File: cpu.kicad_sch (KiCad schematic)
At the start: 24 parts, among them J1 FTSH-105-01-L-DV-K, J24 HTSW-103-07-G-S, U4 CC2745P10, Y2 48MHZ 7PF 20ppm, Y4 32.768KHz 7pF 20ppm

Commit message: Change the cc2745 to a cc2755
Same pinout, cheaper, not automotive.

Signed-off-by: Corey Minyard <corey@minyard.net>
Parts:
- U4: value CC2745P10 -> CC2755P105E0WRHAR; symbol ICs:CC2745P10 -> Local ICs:CC2755P105E0WRHAR
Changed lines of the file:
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@@
 	)
 	(symbol
-		(lib_id "ICs:CC2745P10")
+		(lib_id "Local ICs:CC2755P105E0WRHAR")
 		(at 93.98 92.71 0)
 		(unit 1)
@@
 			)
 		)
-		(property "Value" "CC2745P10"
+		(property "Value" "CC2755P105E0WRHAR"
 			(at 125.73 83.82 0)
 			(effects

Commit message: Add some LEDs
Signed-off-by: Corey Minyard <corey@minyard.net>
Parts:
- added D4: YELLOW LED, LED_SMD:LED_0603_1608Metric_Pad1.05x0.95mm_HandSolder, symbol Device:LED
- added R39: 3KΩ, Resistor_SMD:R_0603_1608Metric_Pad0.98x0.95mm_HandSolder, symbol Device:R
- Y2: value 48MHZ 7PF 20ppm -> Crystal_GND24
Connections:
- net +3.3V: now also D4.2 (A)
- net at U4.3 (DIO0): now also R39.2
- new net: D4.1 (K), R39.1
- no-connect marks 3 -> 2
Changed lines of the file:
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@@
 	)
 	(junction
-		(at 179.07 157.48)
-		(diameter 0)
-		(color 0 0 0 0)
-	)
-	(junction
 		(at 167.64 43.18)
 		(diameter 0)
@@
 	)
 	(no_connect
-		(at 157.48 100.33)
-	)
-	(no_connect
 		(at 264.16 59.69)
 	)
@@
 	(wire
 		(pts
-			(xy 195.58 161.29) (xy 179.07 161.29)
+			(xy 157.48 100.33) (xy 190.5 100.33)
 		)
 		(stroke
@@
 	(wire
 		(pts
-			(xy 161.29 25.4) (xy 161.29 30.48)
+			(xy 195.58 161.29) (xy 179.07 161.29)
 		)
 		(stroke
@@
 	(wire
 		(pts
-			(xy 172.72 151.13) (xy 172.72 152.4)
+			(xy 161.29 25.4) (xy 161.29 30.48)
 		)
 		(stroke
@@
 	(wire
 		(pts
-			(xy 233.68 43.18) (xy 227.33 43.18)
+			(xy 172.72 151.13) (xy 172.72 152.4)
 		)
 		(stroke
@@
 	(wire
 		(pts
-			(xy 161.29 43.18) (xy 161.29 44.45)
+			(xy 233.68 43.18) (xy 227.33 43.18)
 		)
 		(stroke
@@
 	(wire
 		(pts
-			(xy 73.66 128.27) (xy 82.55 128.27)
+			(xy 161.29 43.18) (xy 161.29 44.45)
 		)
 		(stroke
@@
 	(wire
 		(pts
-			(xy 179.07 144.78) (xy 185.42 144.78)
+			(xy 73.66 128.27) (xy 82.55 128.27)
 		)
 		(stroke
@@
 	(wire
 		(pts
+			(xy 209.55 100.33) (xy 217.17 100.33)
+		)
+		(stroke
+			(width 0)
+			(type default)
+		)
+	)
+	(wire
+		(pts
 			(xy 90.17 95.25) (xy 90.17 92.71)
 		)
@@
 	(wire
 		(pts
-			(xy 185.42 144.78) (xy 185.42 146.05)
-		)
-		(stroke
-			(width 0)
-			(type default)
-		)
-	)
-	(wire
-		(pts
 			(xy 74.93 101.6) (xy 81.28 101.6)
 		)
@@
 	(wire
 		(pts
-			(xy 179.07 157.48) (xy 179.07 144.78)
-		)
-		(stroke
-			(width 0)
-			(type default)
-		)
-	)
-	(wire
-		(pts
 			(xy 220.98 38.1) (xy 220.98 43.18)
 		)
@@
 	(wire
 		(pts
+			(xy 217.17 100.33) (xy 217.17 97.79)
+		)
+		(stroke
+			(width 0)
+			(type default)
+		)
+	)
+	(wire
+		(pts
 			(xy 86.36 102.87) (xy 93.98 102.87)
 		)
@@
 	(wire
 		(pts
+			(xy 198.12 100.33) (xy 201.93 100.33)
+		)
+		(stroke
+			(width 0)
+			(type default)
+		)
+	)
+	(wire
+		(pts
 			(xy 54.61 146.05) (xy 93.98 146.05)
 		)
@@
 	)
 	(symbol
+		(lib_id "Device:LED")
+		(at 205.74 100.33 0)
+		(unit 1)
+		(exclude_from_sim no)
+		(in_bom yes)
+		(on_board yes)
+		(dnp no)
+		(property "Reference" "D4"
+			(at 209.042 101.346 0)
+			(effects
+				(font
+					(size 1.27 1.27)
+				)
+			)
+		)
+		(property "Value" "YELLOW LED"
+			(at 206.756 97.79 0)
+			(effects
+				(font
+					(size 1.27 1.27)
+				)
+			)
+		)
+		(property "Footprint" "LED_SMD:LED_0603_1608Metric_Pad1.05x0.95mm_HandSolder"
+			(at 205.74 100.33 0)
+			(effects
+				(font
+					(size 1.27 1.27)
+				)
+				(hide yes)
+			)
+		)
+		(property "Datasheet" "~"
+			(at 205.74 100.33 0)
+			(effects
+				(font
+					(size 1.27 1.27)
+				)
+				(hide yes)
+			)
+		)
+		(property "Description" "Light emitting diode"
+			(at 205.74 100.33 0)
+			(effects
+				(font
+					(size 1.27 1.27)
+				)
+				(hide yes)
+			)
+		)
+		(property "Sim.Pins" "1=K 2=A"
+			(at 205.74 100.33 0)
+			(effects
+				(font
+					(size 1.27 1.27)
+				)
+				(hide yes)
+			)
+		)
+		(pin "1"
+		)
+		(pin "2"
+		)
+		(instances
+			(project "FSKGroundStation"
+				(path "/23e49ab9-97e0-460a-806c-ff6f37958474/f1de8cbf-f219-47ea-9542-15169289ddba"
+					(reference "D4")
+					(unit 1)
+				)
+			)
+		)
+	)
+	(symbol
 		(lib_id "power:GND")
 		(at 74.93 111.76 0)
@@
 	)
 	(symbol
+		(lib_id "power:+3.3V")
+		(at 217.17 97.79 0)
+		(mirror y)
+		(unit 1)
+		(exclude_from_sim no)
+		(in_bom yes)
+		(on_board yes)
+		(dnp no)
+		(fields_autoplaced yes)
+		(property "Reference" "#PWR0151"
+			(at 217.17 101.6 0)
+			(effects
+				(font
+					(size 1.27 1.27)
+				)
+				(hide yes)
+			)
+		)
+		(property "Value" "+3.3V"
+			(at 217.17 92.71 0)
+			(effects
+				(font
+					(size 1.27 1.27)
+				)
+			)
+		)
+		(property "Footprint" ""
+			(at 217.17 97.79 0)
+			(effects
+				(font
+					(size 1.27 1.27)
+				)
+				(hide yes)
+			)
+		)
+		(property "Datasheet" ""
+			(at 217.17 97.79 0)
+			(effects
+				(font
+					(size 1.27 1.27)
+				)
+				(hide yes)
+			)
+		)
+		(property "Description" "Power symbol creates a global label with name \"+3.3V\""
+			(at 217.17 97.79 0)
+			(effects
+				(font
+					(size 1.27 1.27)
+				)
+				(hide yes)
+			)
+		)
+		(pin "1"
+		)
+		(instances
+			(project "FSKGroundStation"
+				(path "/23e49ab9-97e0-460a-806c-ff6f37958474/f1de8cbf-f219-47ea-9542-15169289ddba"
+					(reference "#PWR0151")
+					(unit 1)
+				)
+			)
+		)
+	)
+	(symbol
 		(lib_id "power:GND")
 		(at 195.58 85.09 0)
@@
 			)
 		)
-		(property "Value" "48MHZ 7PF 20ppm"
+		(property "Value" "Crystal_GND24"
 			(at 185.42 143.002 0)
 			(effects
@@
 					(unit 1)
 				)
+			)
+		)
+	)
+	(symbol
+		(lib_id "Device:R")
+		(at 194.31 100.33 270)
+		(unit 1)
+		(exclude_from_sim no)
+		(in_bom yes)
+		(on_board yes)
+		(dnp no)
+		(property "Reference" "R39"
+			(at 194.564 103.124 90)
+			(effects
+				(font
+					(size 1.27 1.27)
+				)
+			)
+		)
+		(property "Value" "3KΩ"
+			(at 194.31 97.79 90)
+			(effects
+				(font
+					(size 1.27 1.27)
+				)
+			)
+		)
+		(property "Footprint" "Resistor_SMD:R_0603_1608Metric_Pad0.98x0.95mm_HandSolder"
+			(at 194.31 98.552 90)
+			(effects
+				(font
+					(size 1.27 1.27)
+				)
+				(hide yes)
+			)
+		)
+		(property "Datasheet" "~"
+			(at 194.31 100.33 0)
+			(effects
+				(font
+					(size 1.27 1.27)
+				)
+				(hide yes)
+			)
+		)
+		(property "Description" "Resistor"
+			(at 194.31 100.33 0)
+			(effects
+				(font
+					(size 1.27 1.27)
+				)
+				(hide yes)
+			)
+		)
+		(pin "2"
+		)
+		(pin "1"
+		)
+		(instances
+			(project "FSKGroundStation"
+				(path "/23e49ab9-97e0-460a-806c-ff6f37958474/f1de8cbf-f219-47ea-9542-15169289ddba"
+					(reference "R39")
+					(unit 1)
+				)

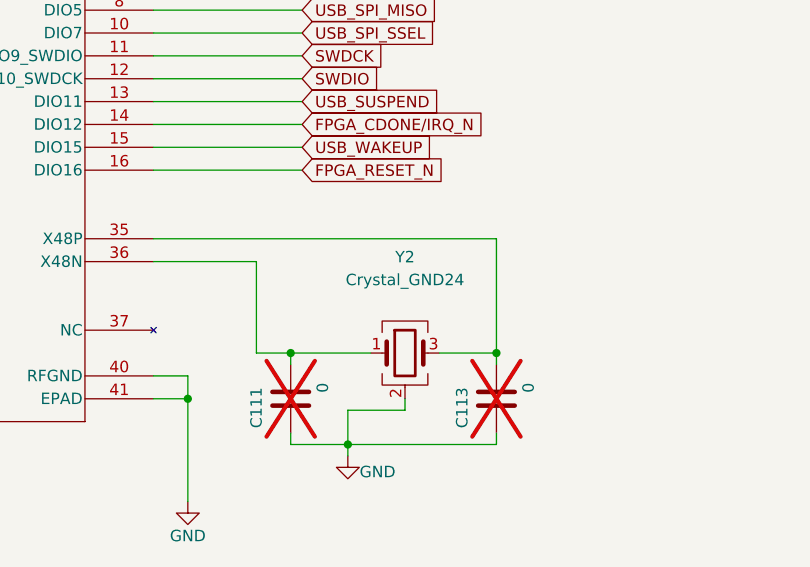
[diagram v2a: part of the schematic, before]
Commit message: Fix some components messed up by the previous change
Signed-off-by: Corey Minyard <corey@minyard.net>
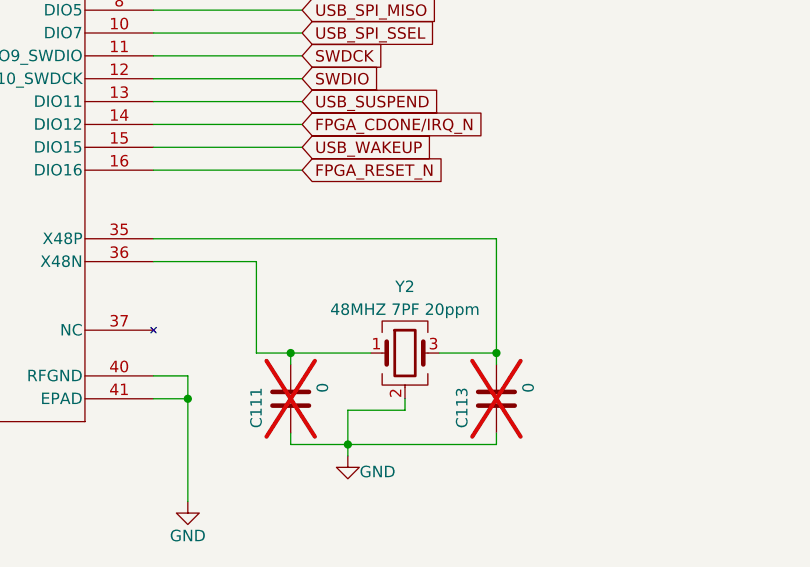
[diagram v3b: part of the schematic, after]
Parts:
- Y2: value Crystal_GND24 -> 48MHZ 7PF 20ppm
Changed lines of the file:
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@@
 		(dnp no)
 		(property "Reference" "Y2"
-			(at 185.42 140.462 0)
+			(at 185.42 143.764 0)
 			(effects
 				(font
@@
 			)
 		)
-		(property "Value" "Crystal_GND24"
-			(at 185.42 143.002 0)
+		(property "Value" "48MHZ 7PF 20ppm"
+			(at 185.42 146.304 0)
 			(effects
 				(font

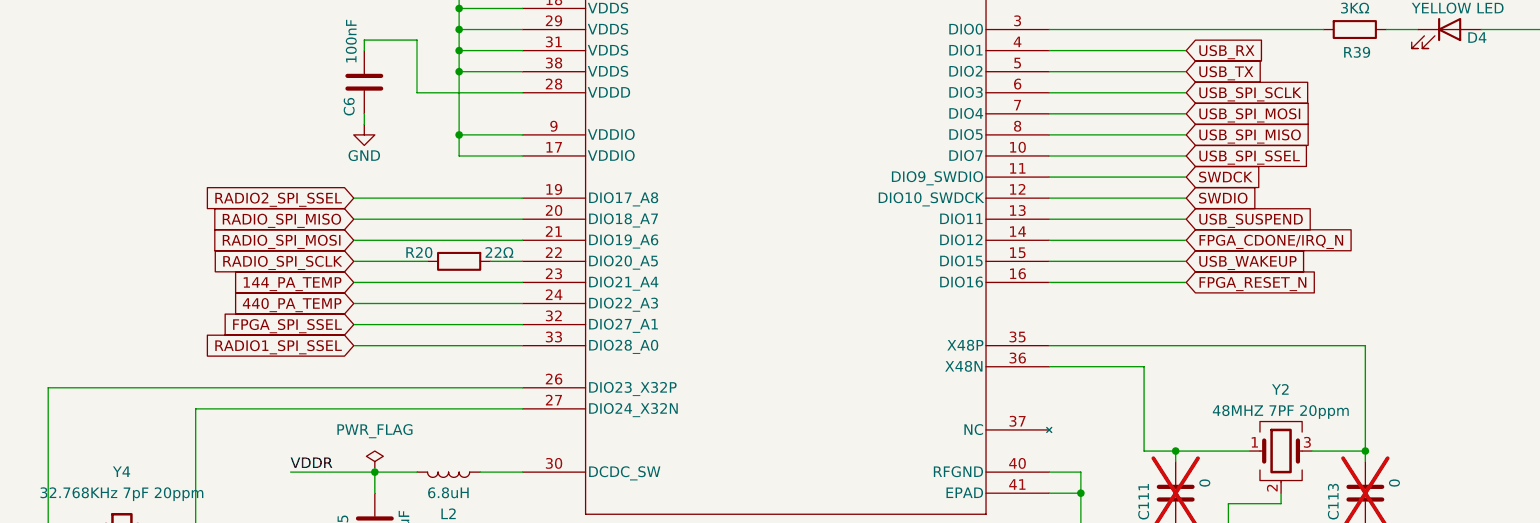
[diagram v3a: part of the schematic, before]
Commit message: Rewire the radio SPI pins
They couldn't go on the pins they were on.

Signed-off-by: Corey Minyard <corey@minyard.net>
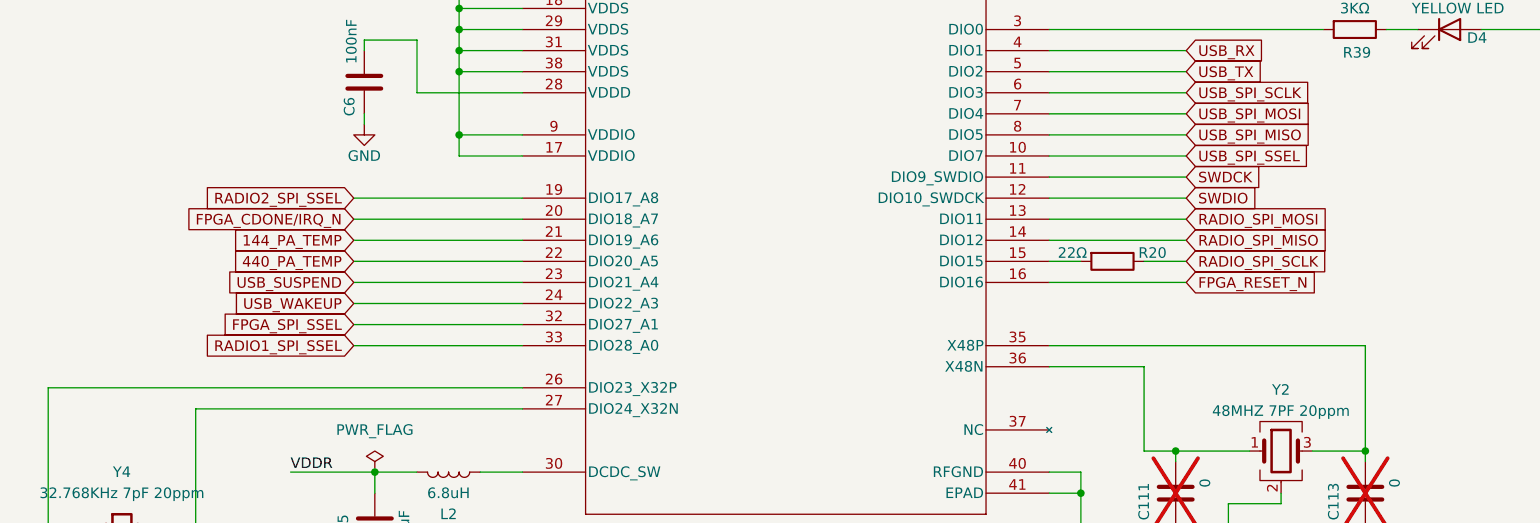
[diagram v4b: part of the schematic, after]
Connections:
- net 144_PA_TEMP: now also U4.21 (DIO19_A6); no longer U4.23 (DIO21_A4)
- net 440_PA_TEMP: now also U4.22 (DIO20_A5); no longer U4.24 (DIO22_A3)
- net FPGA_CDONE/IRQ_N: now also U4.20 (DIO18_A7); no longer U4.14 (DIO12)
- net RADIO_SPI_MISO: now also U4.14 (DIO12); no longer U4.20 (DIO18_A7)
- net RADIO_SPI_MOSI: now also U4.13 (DIO11); no longer U4.21 (DIO19_A6)
- net USB_SUSPEND: now also U4.23 (DIO21_A4); no longer U4.13 (DIO11)
- net USB_WAKEUP: now also U4.24 (DIO22_A3); no longer U4.15 (DIO15)
- net at R20.2: now also U4.15 (DIO15); no longer U4.22 (DIO20_A5)
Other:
- moved on the sheet: R20

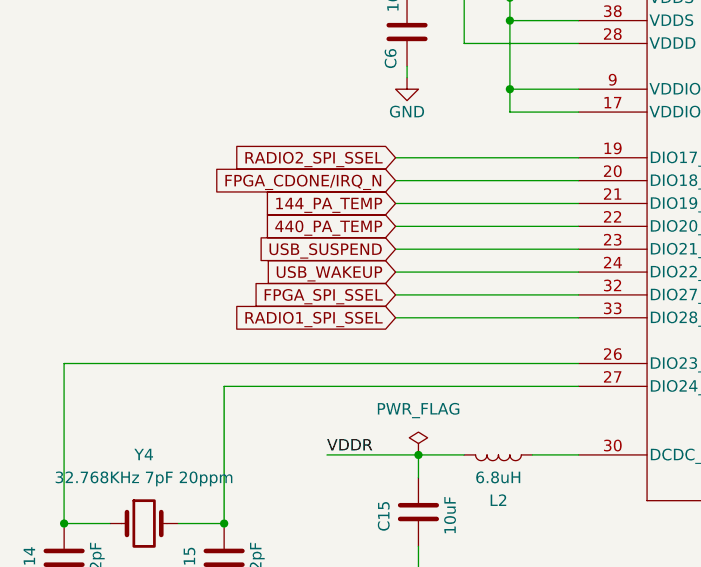
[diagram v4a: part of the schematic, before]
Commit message: More track cleanups for USB and the CPU
Make things a little neater.

Signed-off-by: Corey Minyard <corey@minyard.net>
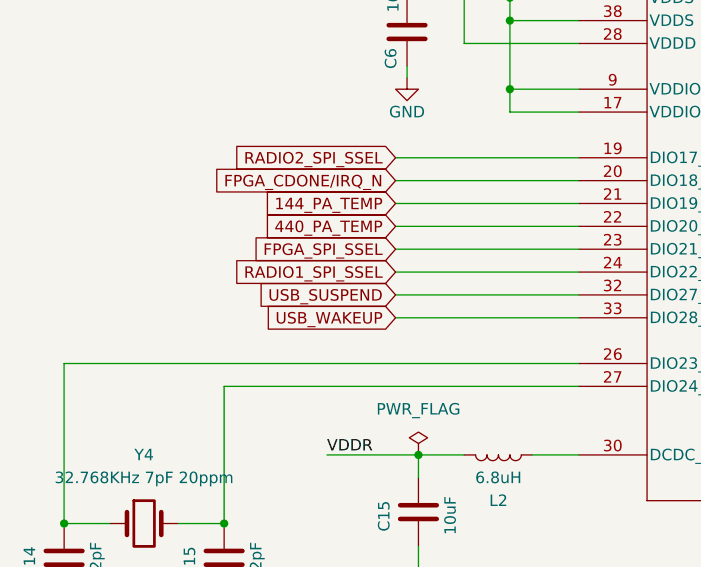
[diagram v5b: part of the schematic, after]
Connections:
- net FPGA_SPI_SSEL: now also U4.23 (DIO21_A4); no longer U4.32 (DIO27_A1)
- net RADIO1_SPI_SSEL: now also U4.24 (DIO22_A3); no longer U4.33 (DIO28_A0)
- net USB_SUSPEND: now also U4.32 (DIO27_A1); no longer U4.23 (DIO21_A4)
- net USB_WAKEUP: now also U4.33 (DIO28_A0); no longer U4.24 (DIO22_A3)

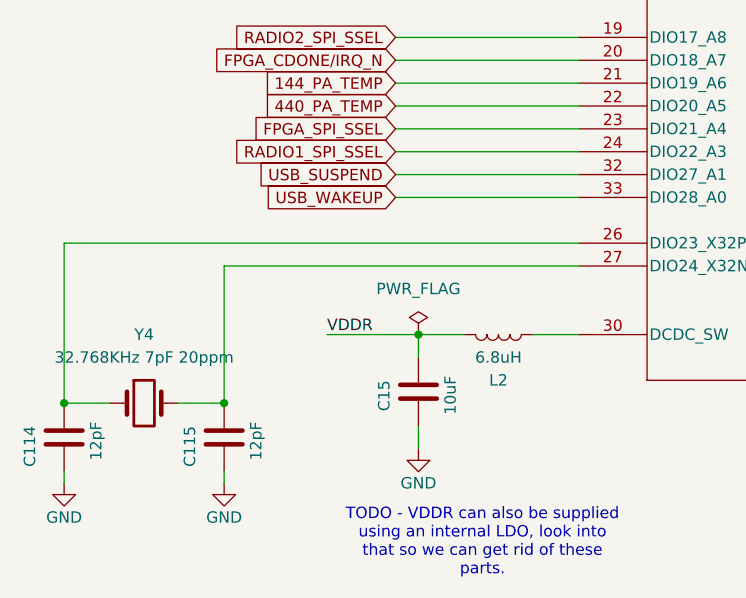
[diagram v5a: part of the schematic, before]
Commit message: Switch to a CPU with a USB interface for the USB connection
The part that was picked had proprietary tools and configuration and it
didn't support interrupts.  The CPU is cheaper and more capable.

Signed-off-by: Corey Minyard <corey@minyard.net>
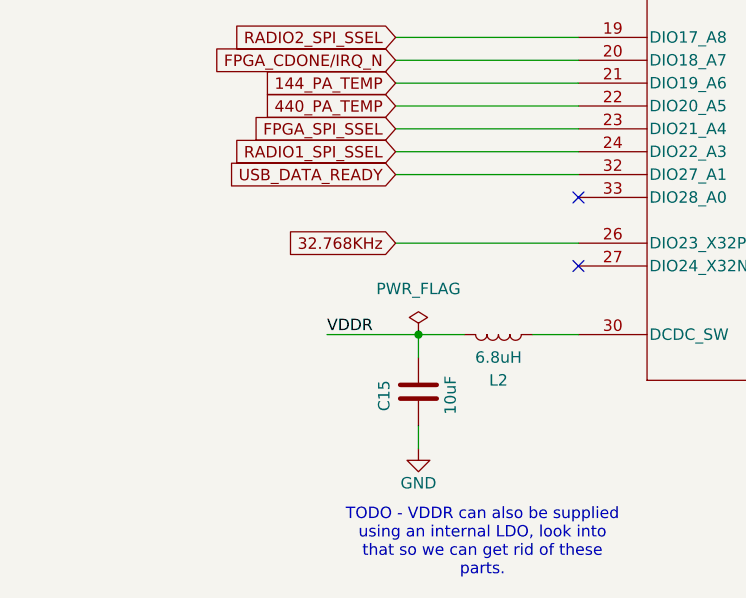
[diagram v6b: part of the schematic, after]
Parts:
- removed C114, C115: 12pF, Capacitor_SMD:C_0402_1005Metric_Pad0.74x0.62mm_HandSolder, symbol Device:C
- removed Y4: 32.768KHz 7pF 20ppm, Crystal:Crystal_SMD_2012-2Pin_2.0x1.2mm, symbol Device:Crystal
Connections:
- net 32.768KHz: now reaches U4.26 (DIO23_X32P)
- net USB_SUSPEND renamed USB_DATA_READY
- net USB_WAKEUP: no longer names the net of U4.33 (DIO28_A0)
- no-connect marks 2 -> 4

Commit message: Add a clock from the USB chip to the FPGA
The FPGA might need a clock for certain things, so provide it.

Signed-off-by: Corey Minyard <corey@minyard.net>
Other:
- note added: "The USB interface provides a 32.768KHz clock, we use that here."
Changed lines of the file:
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@@
+		)
+	)
+	(text "The USB interface provides a\n32.768KHz clock, we use that\nhere."
+		(exclude_from_sim no)
+		(at 44.45 144.272 0)
+		(effects
+			(font
+				(size 1.27 1.27)
+			)
 		)
 	)

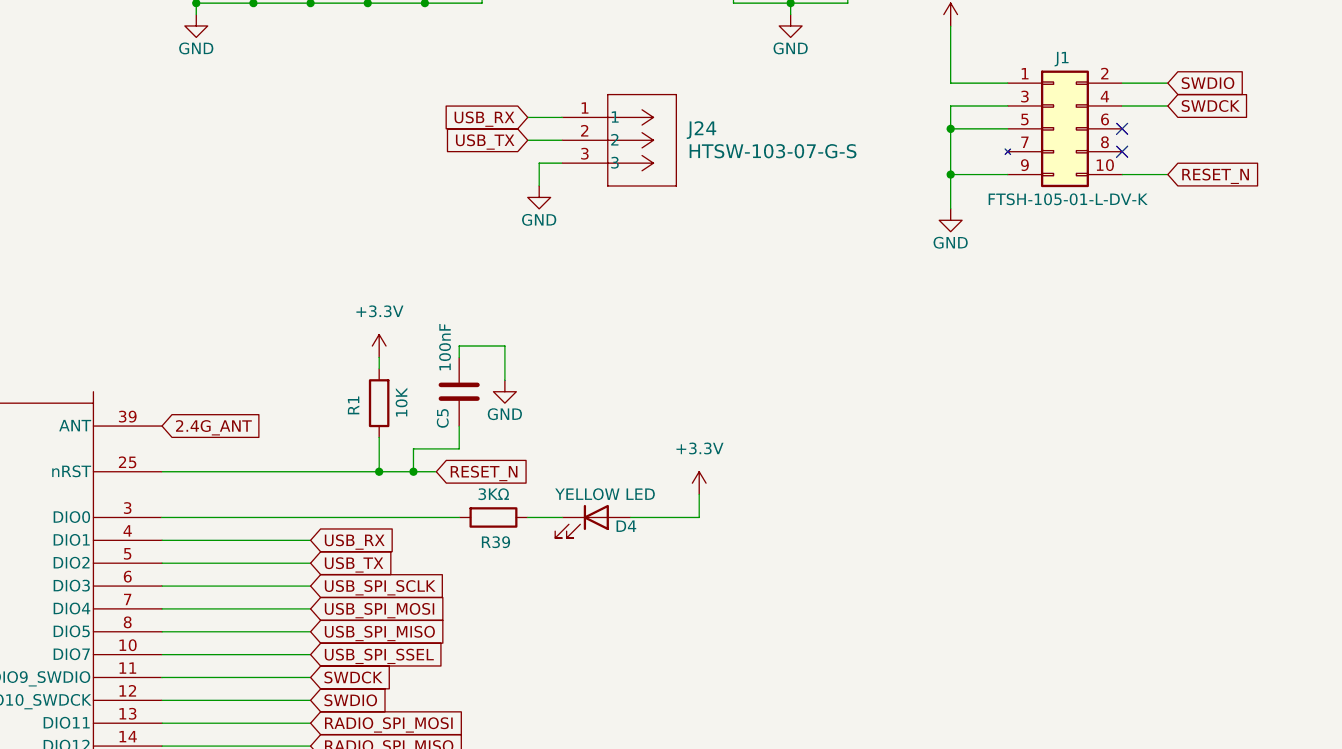
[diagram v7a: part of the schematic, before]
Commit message: Split the USB CPU and main CPU reset lines
Signed-off-by: Corey Minyard <corey@minyard.net>
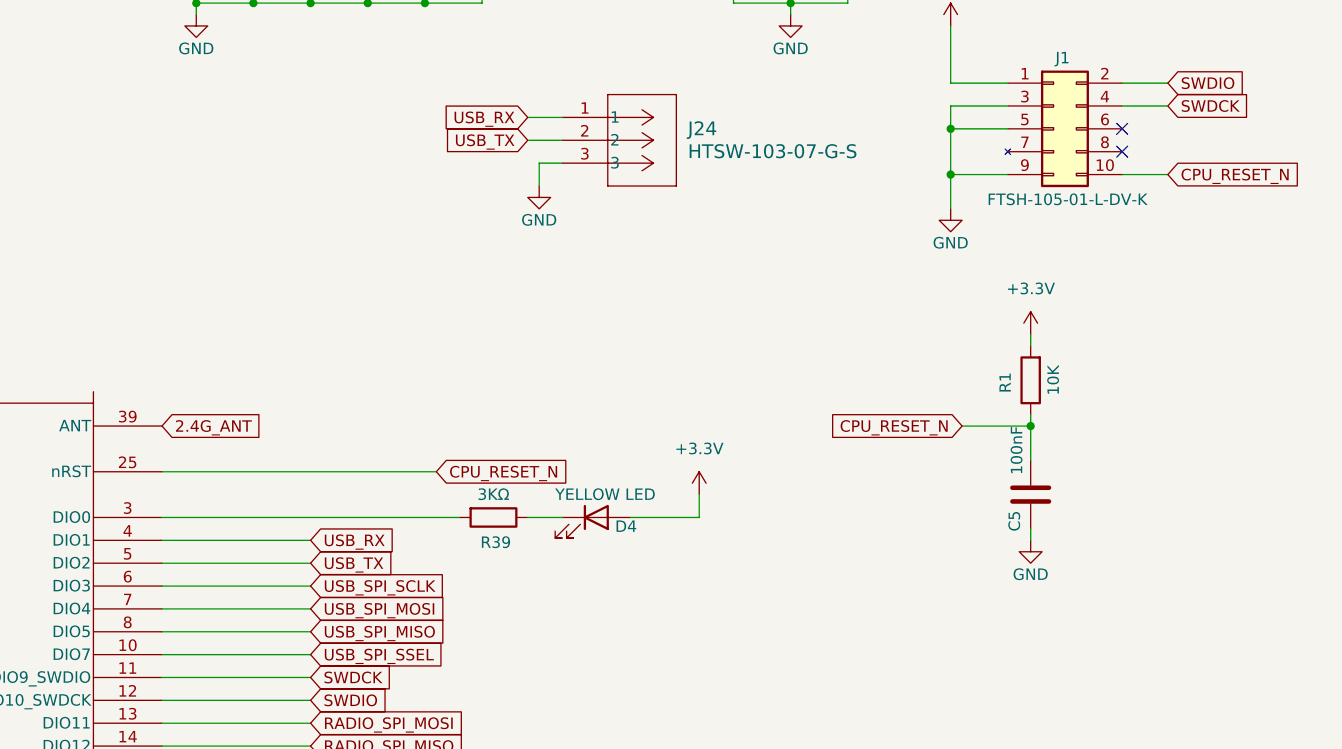
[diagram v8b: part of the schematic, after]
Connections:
- net GND: now also C5.1; no longer C5.2
- net RESET_N renamed CPU_RESET_N
- net CPU_RESET_N: now also C5.2; no longer C5.1
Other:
- moved on the sheet: C5, R1
